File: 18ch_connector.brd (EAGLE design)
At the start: 7.5 x 6.7 mm, 1 part, among them X1 OMNETIC_18PAD

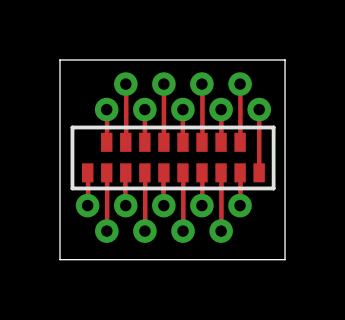
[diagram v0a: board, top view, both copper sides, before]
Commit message: added component values
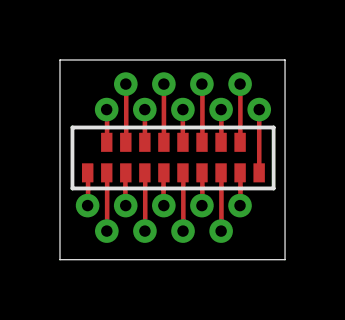
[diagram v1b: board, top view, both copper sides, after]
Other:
- board outline removed
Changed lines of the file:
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@@
 <?xml version="1.0" encoding="utf-8"?>
 <!DOCTYPE eagle SYSTEM "eagle.dtd">
-<eagle version="6.5.0">
+<eagle version="6.6.0">
 <drawing>
 <settings>
@@
 <board>
 <plain>
-<wire x1="0" y1="0.003" x2="7.501" y2="0.003" width="0" layer="20"/>
-<wire x1="7.501" y1="0.003" x2="7.501" y2="6.659" width="0" layer="20"/>
-<wire x1="7.501" y1="6.659" x2="0" y2="6.659" width="0" layer="20"/>
-<wire x1="0" y1="6.659" x2="0" y2="0.003" width="0" layer="20"/>
+<wire x1="0" y1="0.003" x2="7.501" y2="0.003" width="0" layer="21"/>
+<wire x1="7.501" y1="0.003" x2="7.501" y2="6.659" width="0" layer="21"/>
+<wire x1="7.501" y1="6.659" x2="0" y2="6.659" width="0" layer="21"/>
+<wire x1="0" y1="6.659" x2="0" y2="0.003" width="0" layer="21"/>
+<wire x1="0.000509375" y1="0.002665625" x2="7.50049375" y2="0.002665625" width="0" layer="22"/>
+<wire x1="7.50049375" y1="0.002665625" x2="7.50049375" y2="6.65924375" width="0" layer="22"/>
+<wire x1="7.50049375" y1="6.65924375" x2="0" y2="6.65924375" width="0" layer="22"/>
+<wire x1="0" y1="6.65924375" x2="0" y2="0.002159375" width="0" layer="22"/>
 </plain>
 <attributes>
